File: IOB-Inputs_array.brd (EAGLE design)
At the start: 104.1 x 106.7 mm, 83 parts, among them J1X11 RJ12/6, J1X12 RJ12/6, J1X13 RJ12/6, J1X14 RJ12/6

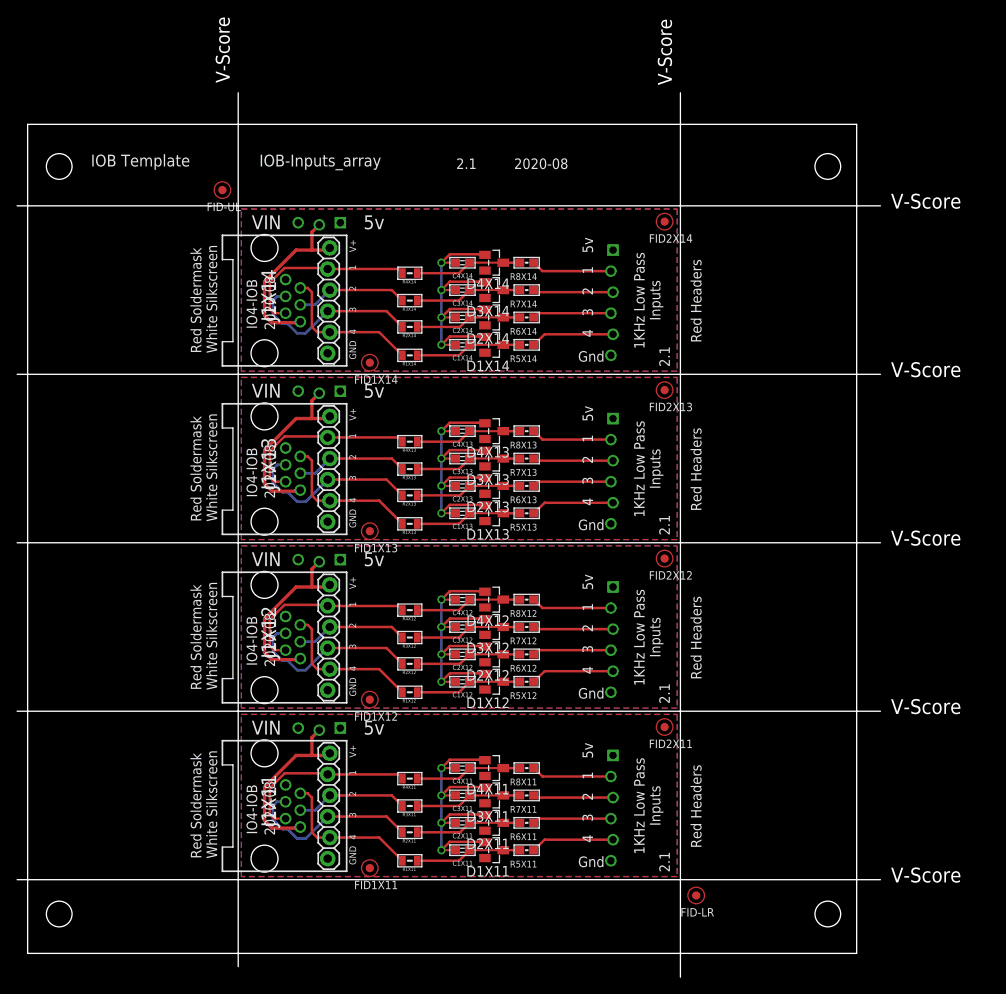
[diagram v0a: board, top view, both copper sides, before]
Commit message: Moved 82R inline with others
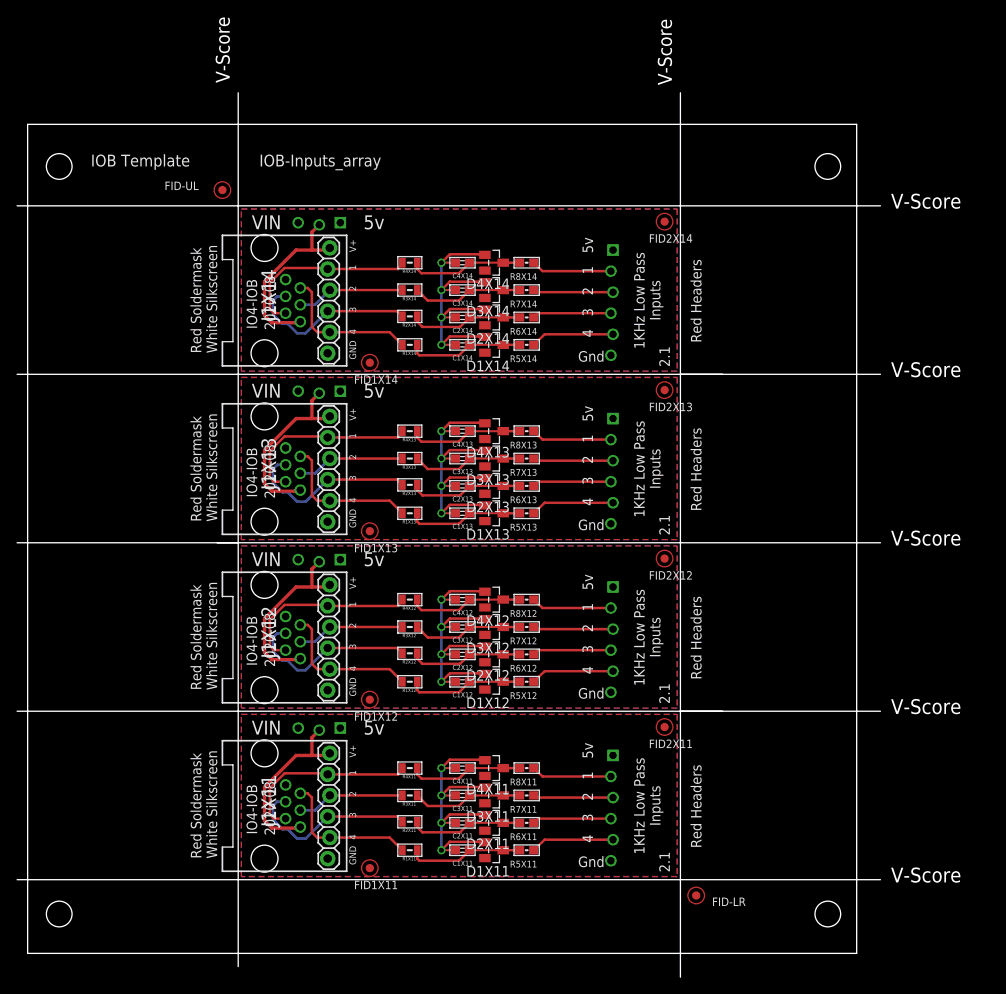
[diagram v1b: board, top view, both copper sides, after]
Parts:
- moved R1X14 1.27 mm to (46.1, 73.4)
- moved R3X14 1.27 mm to (46.1, 80.0)
- moved R2X12 1.27 mm to (46.1, 36.2)
- moved R2X13 1.27 mm to (46.1, 56.5)
- moved R1X11 1.27 mm to (46.1, 12.4)
- moved R1X12 1.27 mm to (46.1, 32.8)
- moved R2X11 1.27 mm to (46.1, 15.9)
- moved R3X11 1.27 mm to (46.1, 19.1)
- moved R4X11 1.27 mm to (46.1, 22.4)
- moved R1X13 1.27 mm to (46.1, 53.1)
- moved R2X14 1.27 mm to (46.1, 76.8)
- moved R3X12 1.27 mm to (46.1, 39.4)
- moved R3X13 1.27 mm to (46.1, 59.7)
- moved R4X12 1.27 mm to (46.1, 42.7)
- moved R4X13 1.27 mm to (46.1, 63.0)
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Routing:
- net N$10X14: track 12.9 -> 14.0 mm
- net N$10X13: track 12.9 -> 14.0 mm
- net N$10X12: track 12.9 -> 14.0 mm
- net N$10X11: track 12.9 -> 14.0 mm
- net N$14X11: track 12.9 -> 13.9 mm
- net N$14X14: track 12.9 -> 13.9 mm
- net N$14X13: track 12.9 -> 13.9 mm
- net N$14X12: track 12.9 -> 13.9 mm
- net N$12X13: track 12.8 -> 13.7 mm
- net N$12X12: track 12.8 -> 13.7 mm
- net N$12X11: track 12.8 -> 13.7 mm
- net N$12X14: track 12.8 -> 13.7 mm
- net N$13X14: track 12.9 -> 13.4 mm
- net N$13X13: track 12.9 -> 13.4 mm
- net N$13X12: track 12.9 -> 13.4 mm
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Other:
- board text added: "R1"
- board text added: "R2"
- board text added: "R3"
- board text added: "R4"
- board text removed: "R10"
- board text removed: "R11"
- board text removed: "R12"
- board text removed: "R9"
